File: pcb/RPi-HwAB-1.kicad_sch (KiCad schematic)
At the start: 7 parts, among them J1 GPIO, J2 Hirose_FH12-16S, U1 CAT24C256

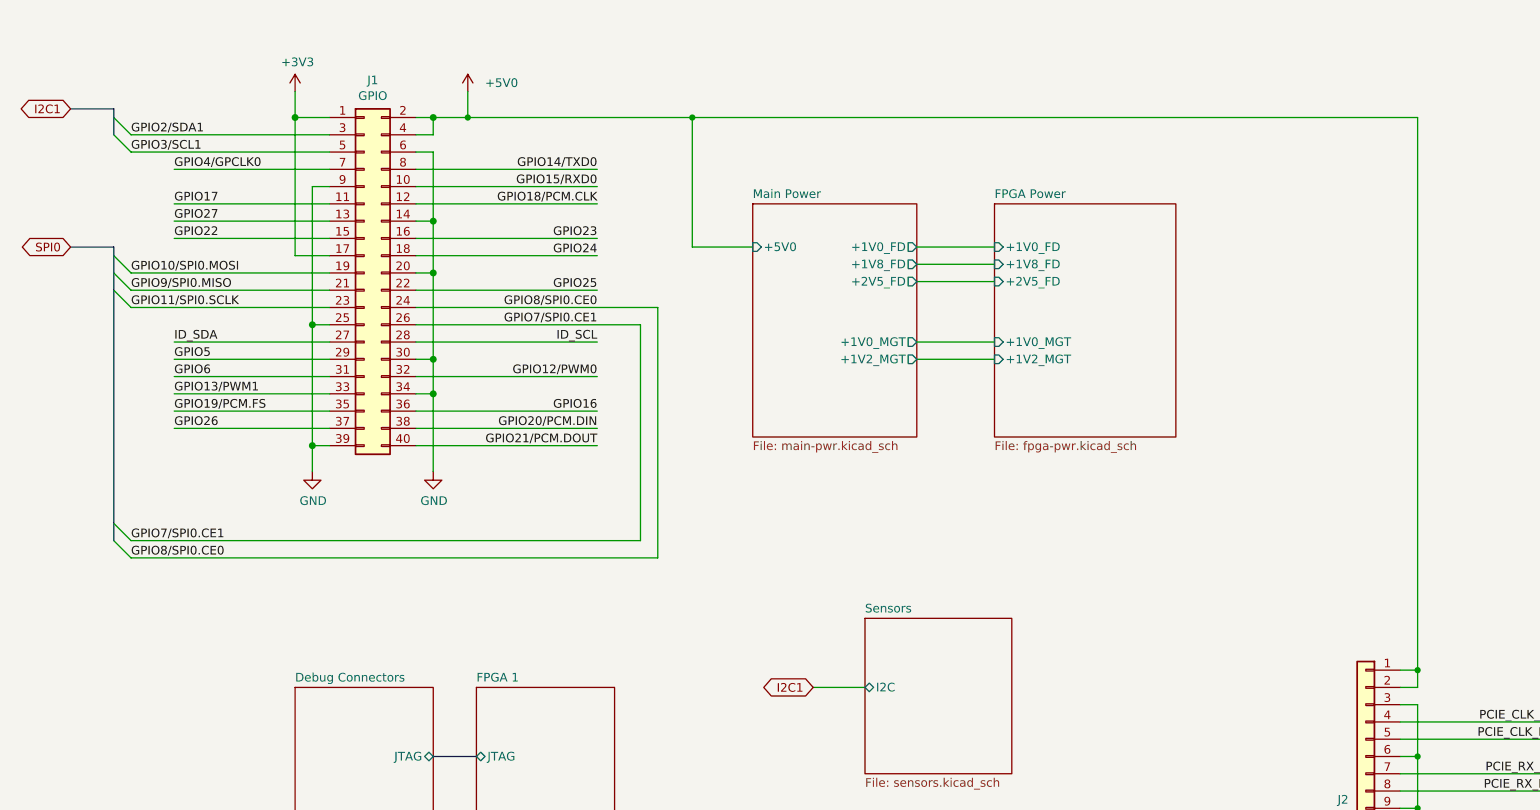
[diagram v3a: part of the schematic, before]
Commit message: added power sequencing through raspi gpio
additionally defined sensors
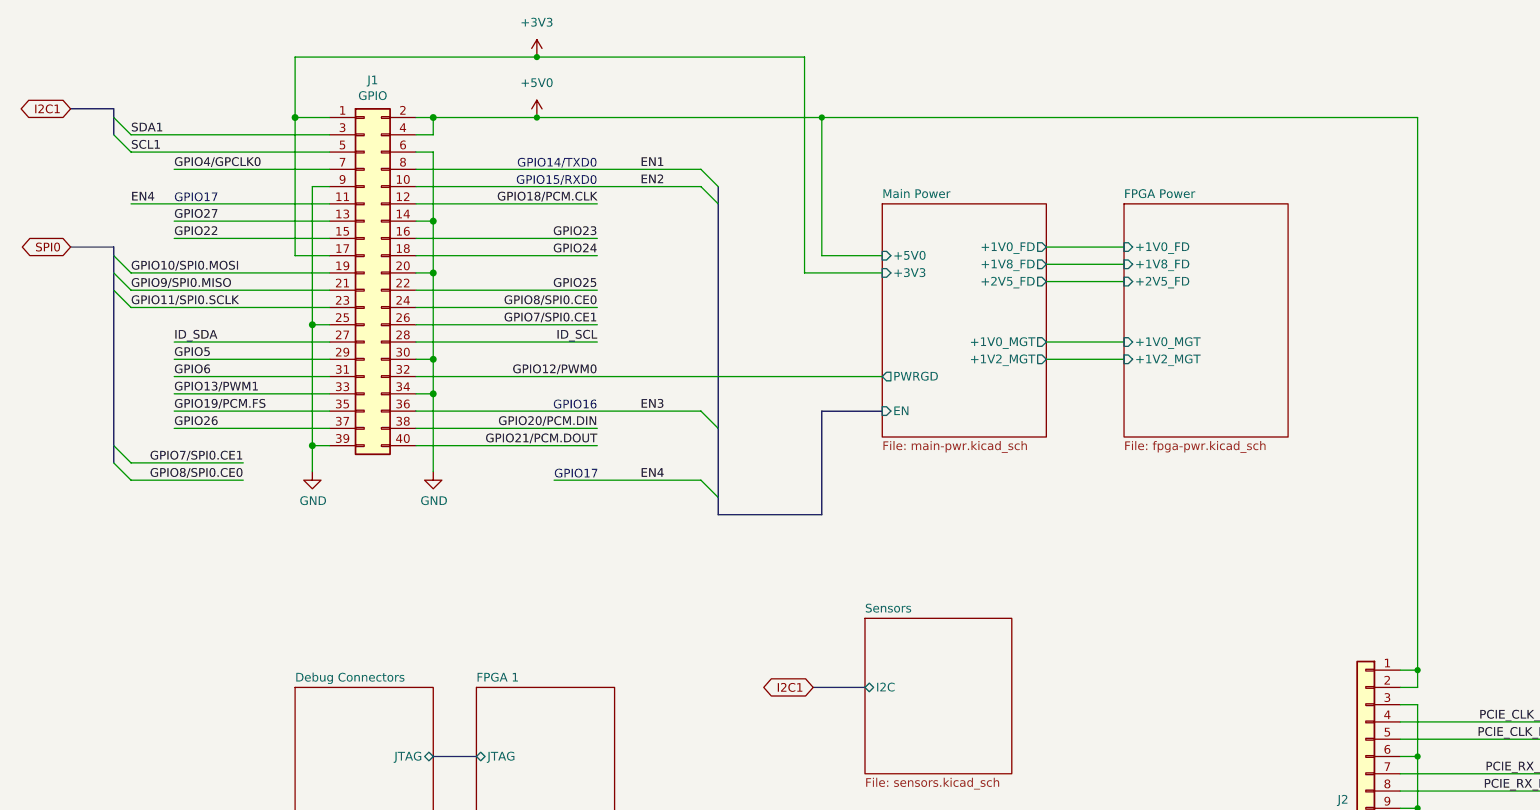
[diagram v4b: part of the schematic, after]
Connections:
- net GPIO14/TXD0 renamed EN1
- net GPIO15/RXD0 renamed EN2
- net GPIO16 renamed EN3
- net GPIO17 renamed EN4
- net GPIO2/SDA1 renamed SDA1
- net GPIO3/SCL1 renamed SCL1
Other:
- sheet Main Power ports: added +3V3, EN, PWRGD; removed none
- note added: "GPIO14/TXD0"
- note added: "GPIO15/RXD0"
- note added: "GPIO16"
- note added: "GPIO17"
- company: (none) -> Andre S Winkel
- title: (none) -> RPi HwAB HAT+

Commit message: quick edits to hierarchy
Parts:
- C1: footprint (none) -> Capacitor_SMD:C_0402_1005Metric
- J2: footprint Connector_FFC-FPC:Hirose_FH12-16S-0.5SH_1x16-1MP_P0.50mm_Horizontal -> Connector_FFC-FPC:Hirose_FH12-17S-0.5SH_1x17-1MP_P0.50mm_Horizontal
- JP1: footprint (none) -> Jumper:SolderJumper-2_P1.3mm_Open_Pad1.0x1.5mm
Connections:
- net PCIE_RX_N: now also J2.11 (Pin_11); no longer J2.8 (Pin_8)
- net PCIE_RX_P: now also J2.10 (Pin_10); no longer J2.7 (Pin_7)
- net PCIE_TX_N: now also J2.8 (Pin_8); no longer J2.11 (Pin_11)
- net PCIE_TX_P: now also J2.7 (Pin_7); no longer J2.10 (Pin_10)
- net EN1 renamed GPIO14/TXD0
- net EN2 renamed GPIO15/RXD0
- net EN3 renamed GPIO16
- net EN4 renamed GPIO17
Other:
- sheet FPGA 3 ports: added PCIE_CLKREQ_N, PCIE_CLK_N, PCIE_CLK_P, PCIE_DET_WAKE, PCIE_PWR_EN, PCIE_RST_B, PCIE_RX_N, PCIE_RX_P, PCIE_TX_N, PCIE_TX_P; removed PCIE, PCIE_AUX
- sheet Main Power ports: added EN1, EN2, EN3, EN4; removed EN
- sheet Sensors ports: added SCL1, SDA1; removed I2C
- note added: "note: tx here is rx on raspi, etc."
- note removed: "GPIO14/TXD0"
- note removed: "GPIO15/RXD0"
- note removed: "GPIO16"
- note removed: "GPIO17"

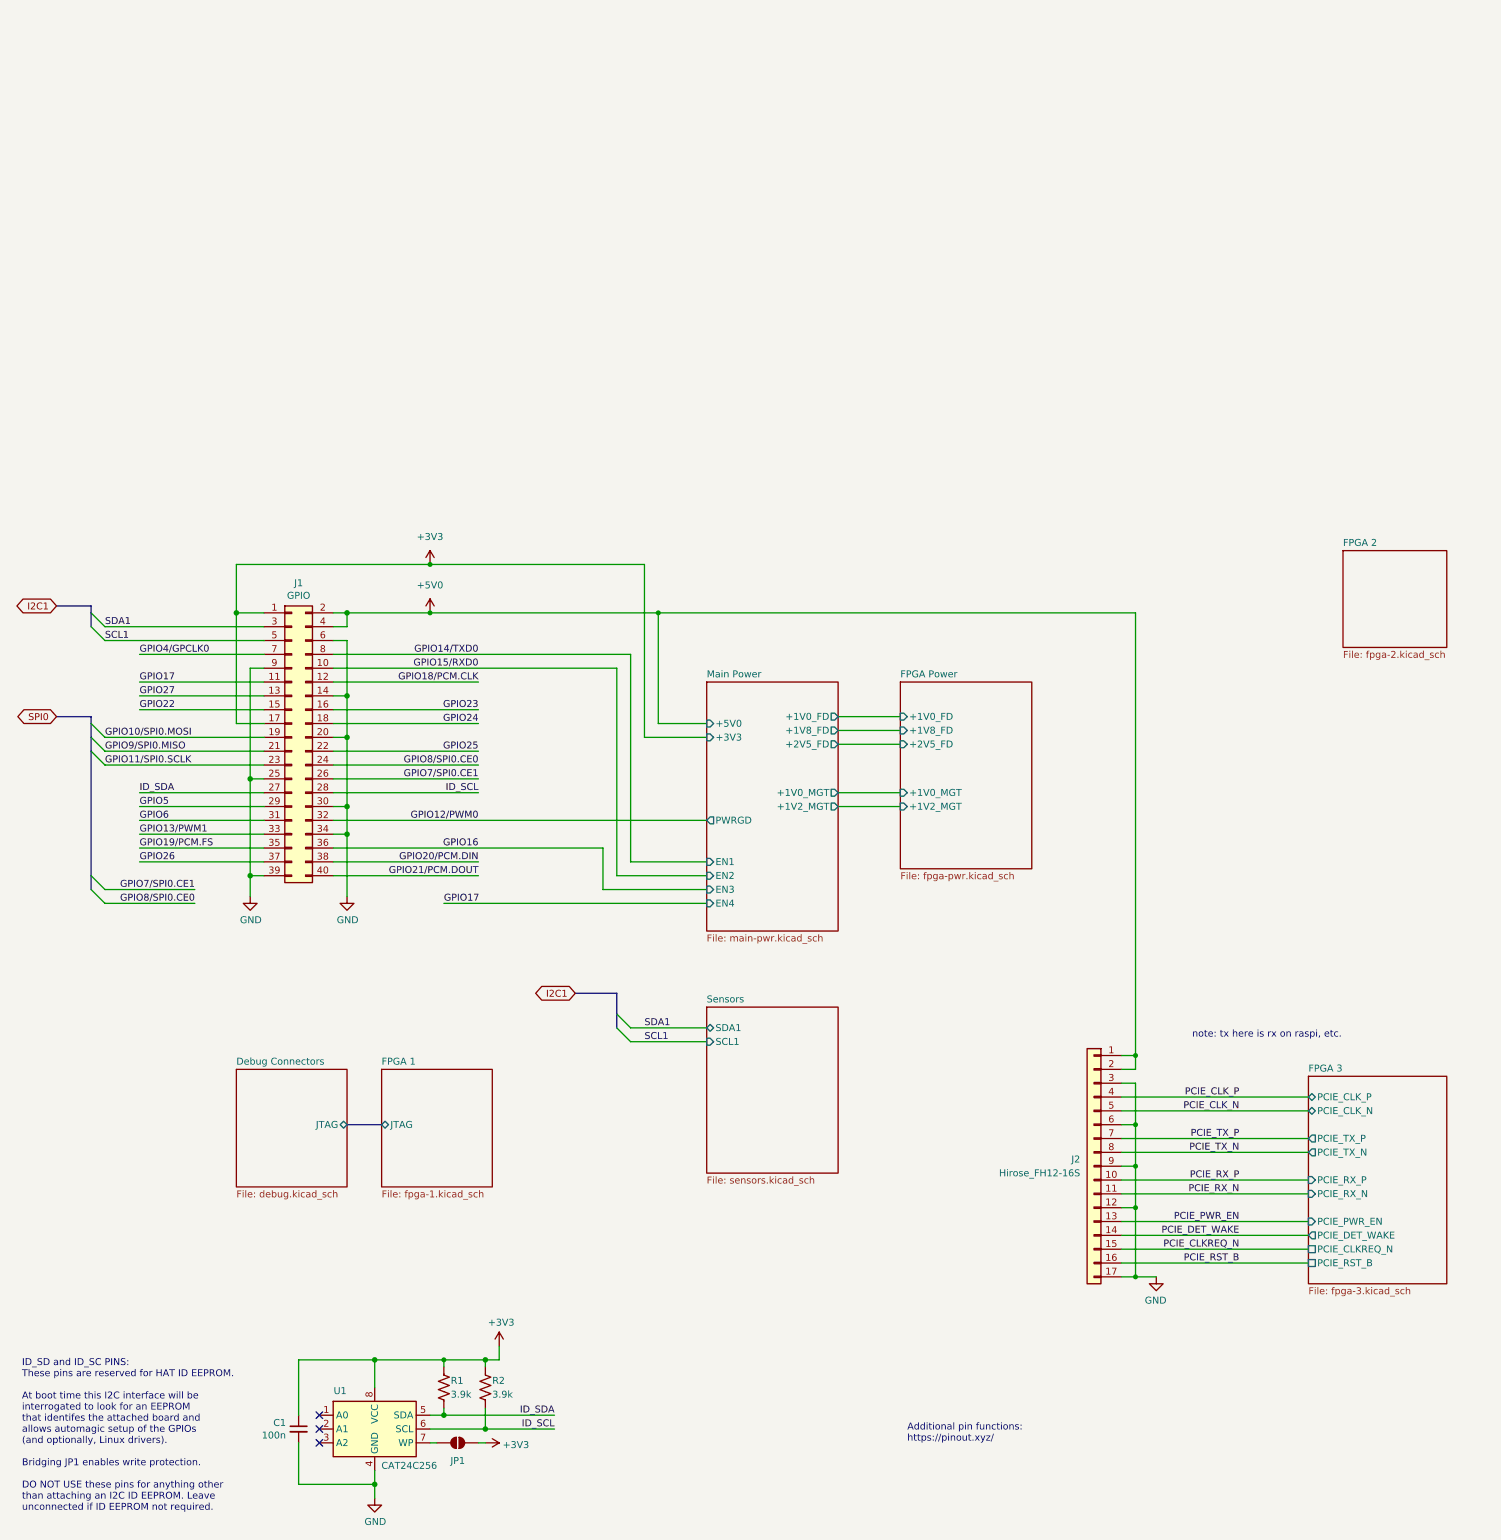
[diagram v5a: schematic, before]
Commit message: added power supply simulations
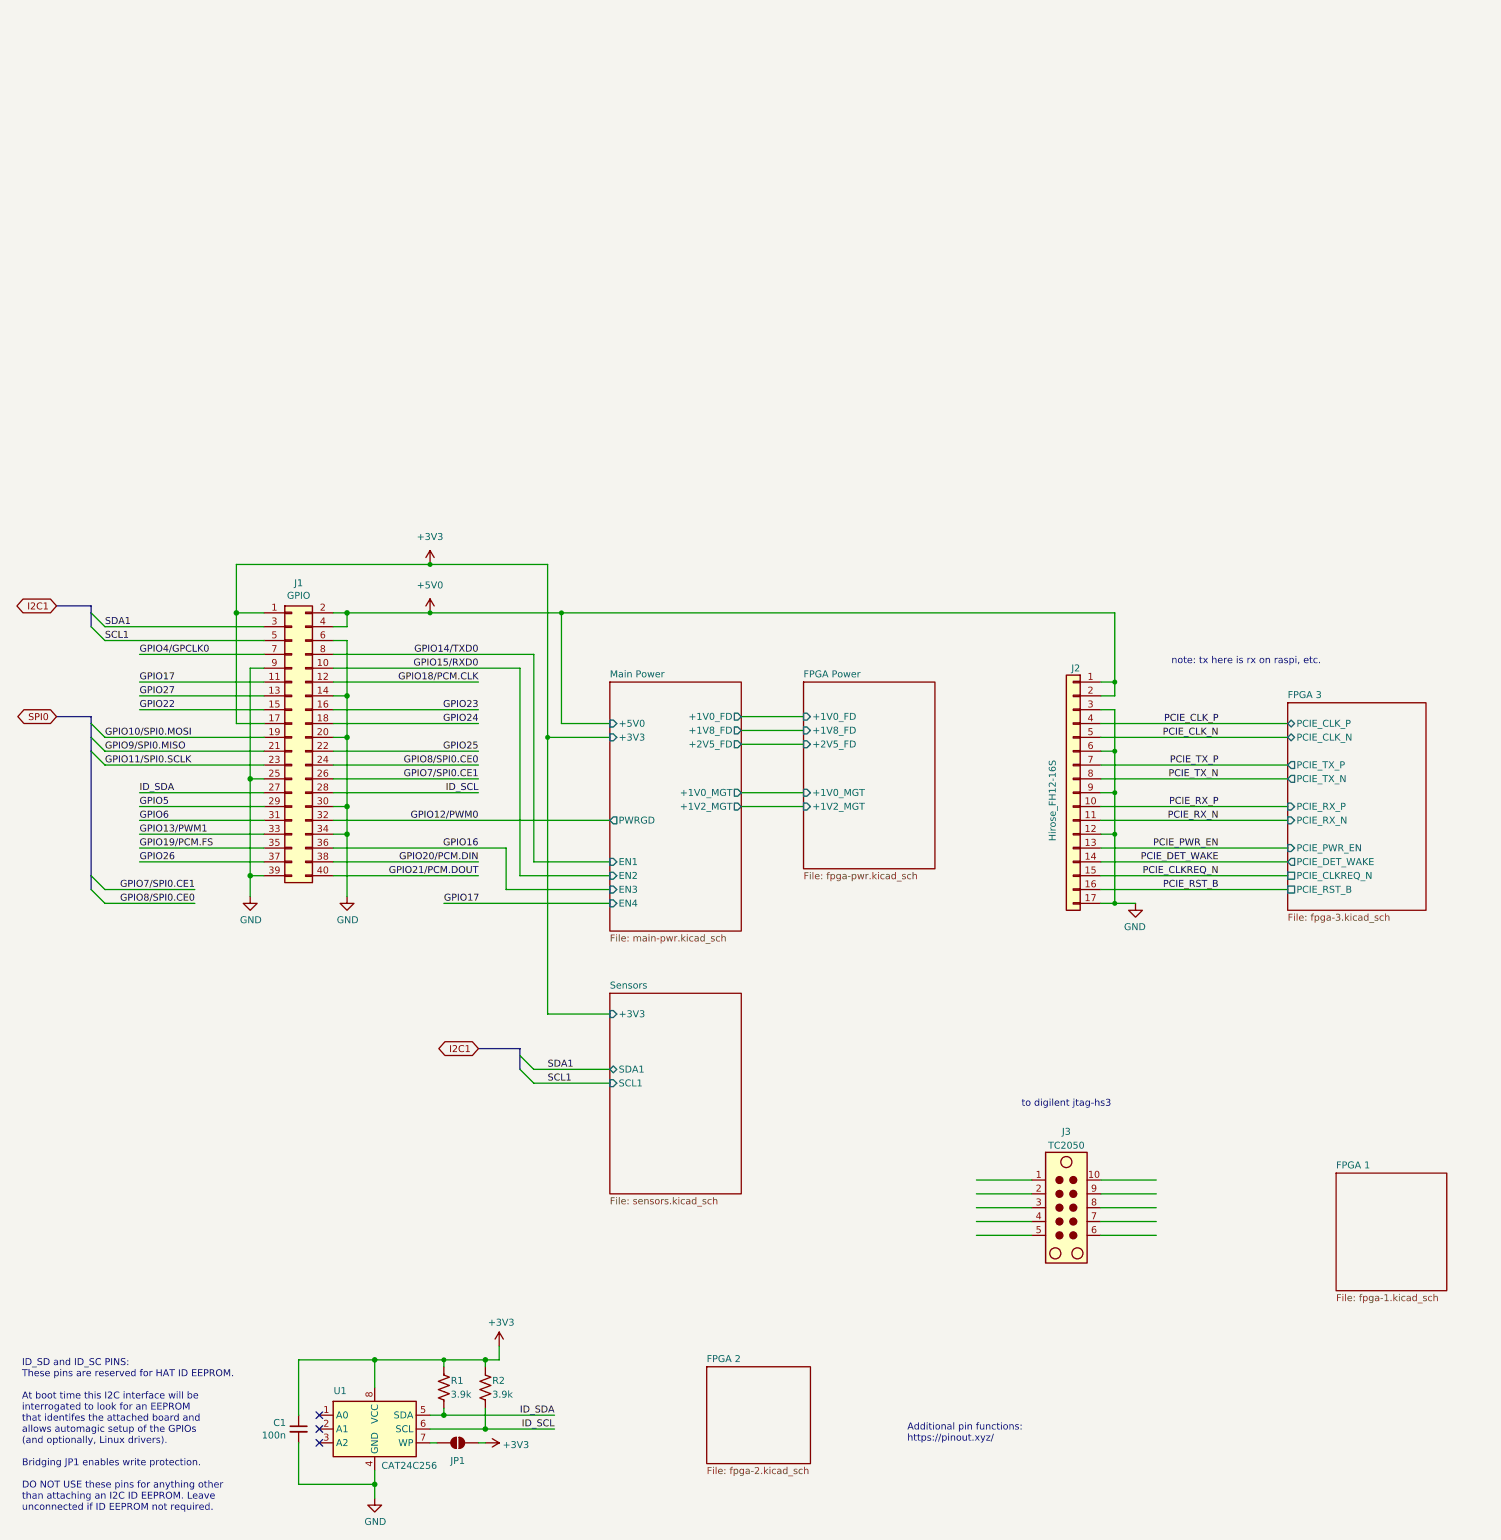
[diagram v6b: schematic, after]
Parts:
- added J3: TC2050, Connector:Tag-Connect_TC2050-IDC-NL_2x05_P1.27mm_Vertical, symbol Connector:TC2050
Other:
- removed sheet Debug Connectors
- sheet FPGA 1 ports: added none; removed JTAG
- sheet Sensors ports: added +3V3; removed none
- note added: "to digilent jtag-hs3"
- moved on the sheet: J2

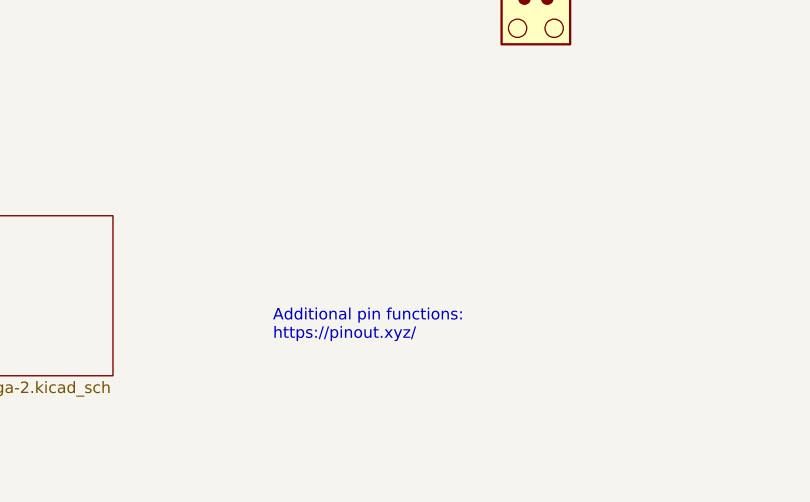
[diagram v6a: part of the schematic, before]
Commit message: defined pcie diff. connections
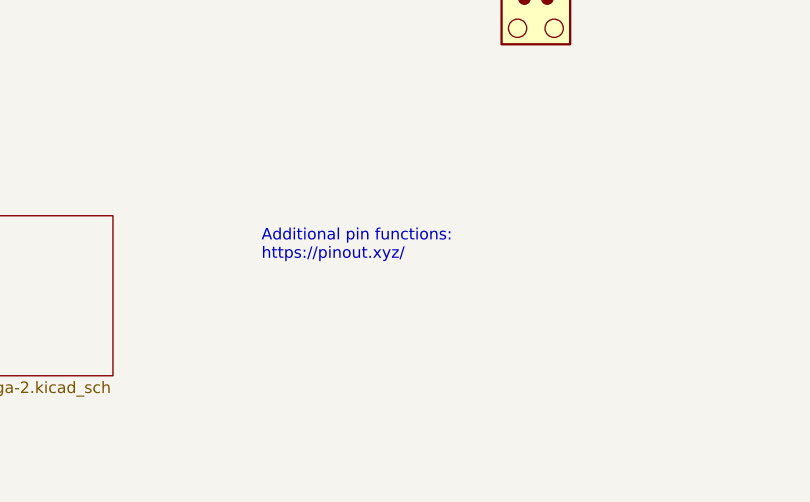
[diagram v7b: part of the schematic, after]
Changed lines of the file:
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@@
 	(text "Additional pin functions:\nhttps://pinout.xyz/"
 		(exclude_from_sim no)
-		(at 179.07 180.34 0)
+		(at 177.8 171.45 0)
 		(effects
 			(font
